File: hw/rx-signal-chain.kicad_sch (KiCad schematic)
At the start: 41 parts, among them T301 BN-43-202, 200 : 3-way 50 ohm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, U301 OPA1692xDGK, U302 SN74LVC04APW, U303 AK5578EN

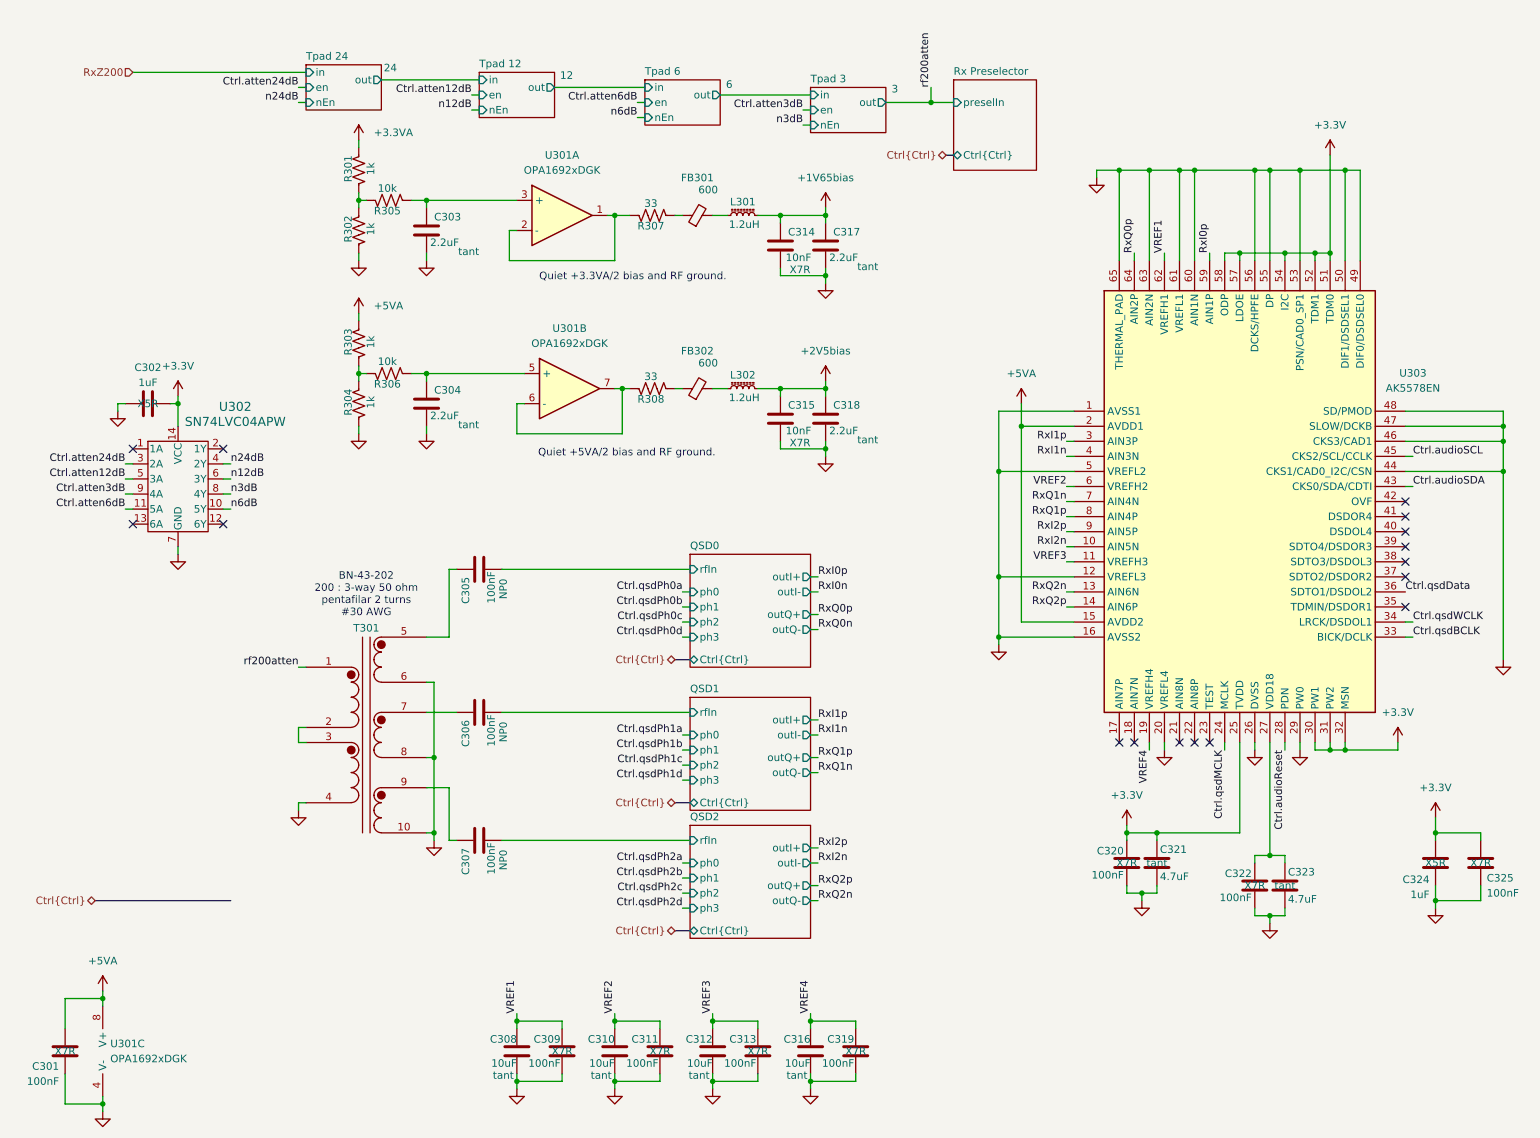
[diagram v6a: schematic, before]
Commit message: All ERC pass. Import to PCB works with no footprints missing.
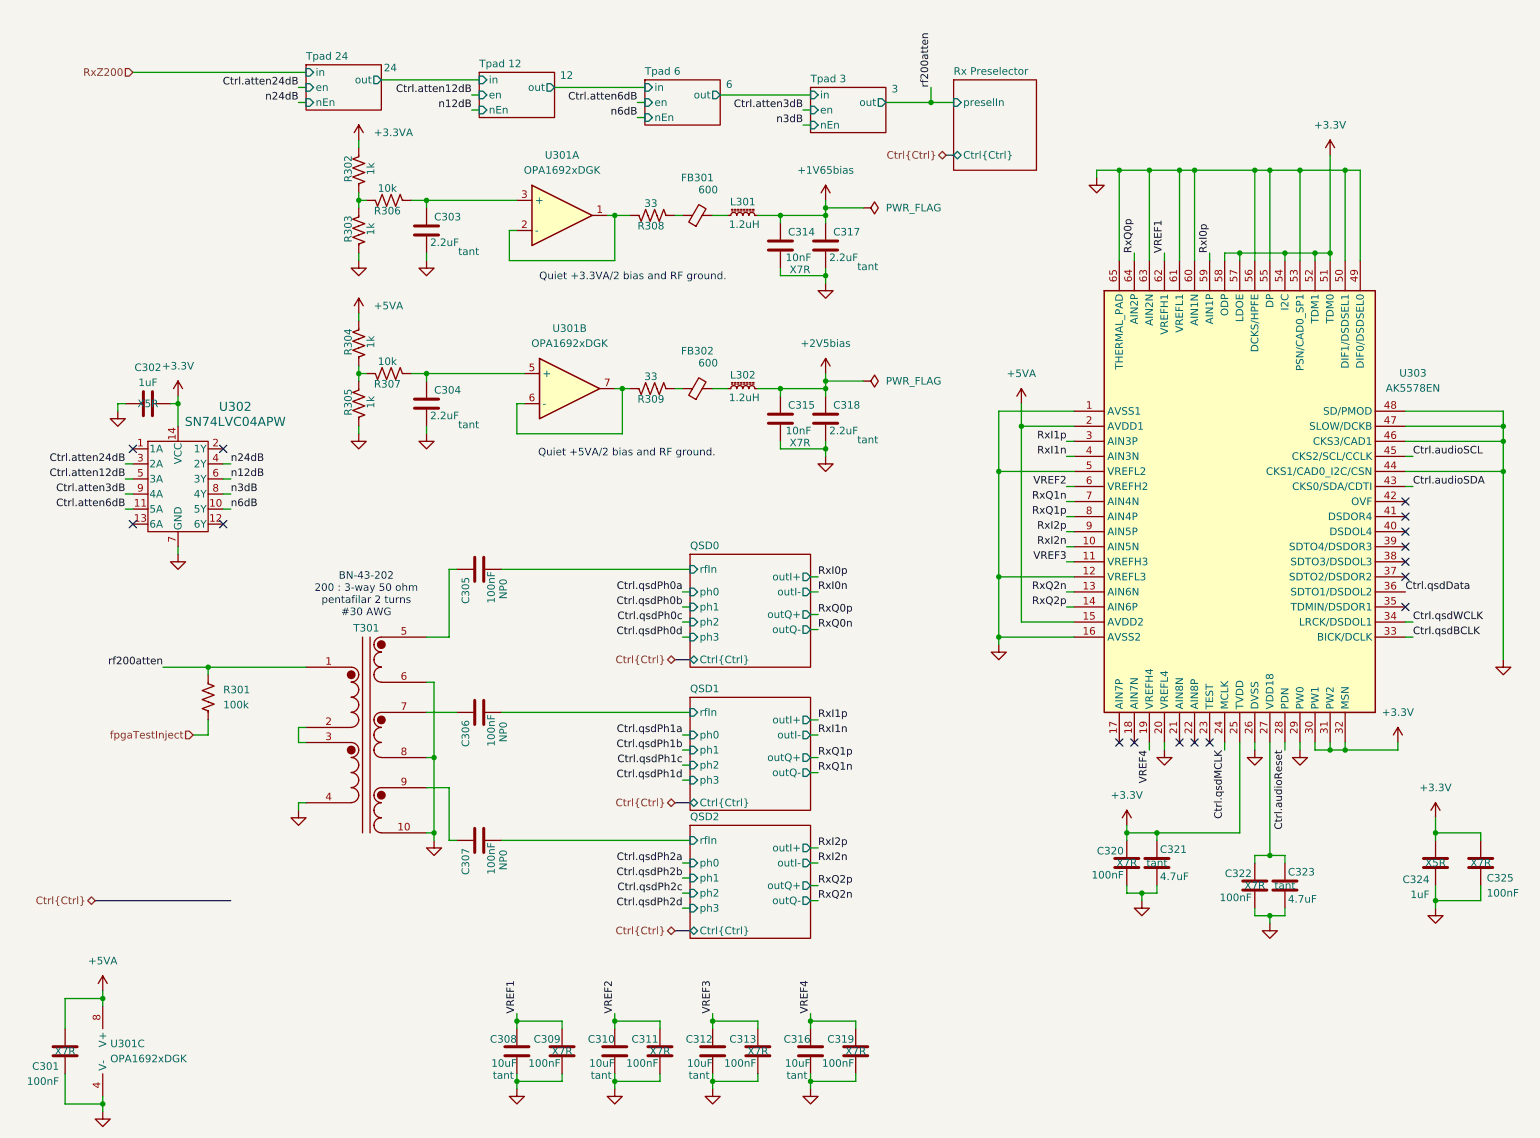
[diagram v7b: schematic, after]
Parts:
- added R301: 100k, Resistor_SMD:R_0402_1005Metric, symbol Device:R_US
- U302: footprint PW14 -> Library:PW14
- U303: symbol AK5578EN:AK5578EN -> Library:AK5578EN
- renumbered R301 to R302, R302 to R303, R303 to R304, R304 to R305, R305 to R306, R306 to R307, R307 to R308, R308 to R309
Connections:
- net rf200atten: now also R301.1
- new net fpgaTestInject: R301.2

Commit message: Checkpoint. Now using TQFP100 STM32H753VIT6, no longer using SPI expanders to drive controls for L,C,atten. FPGA does that now.
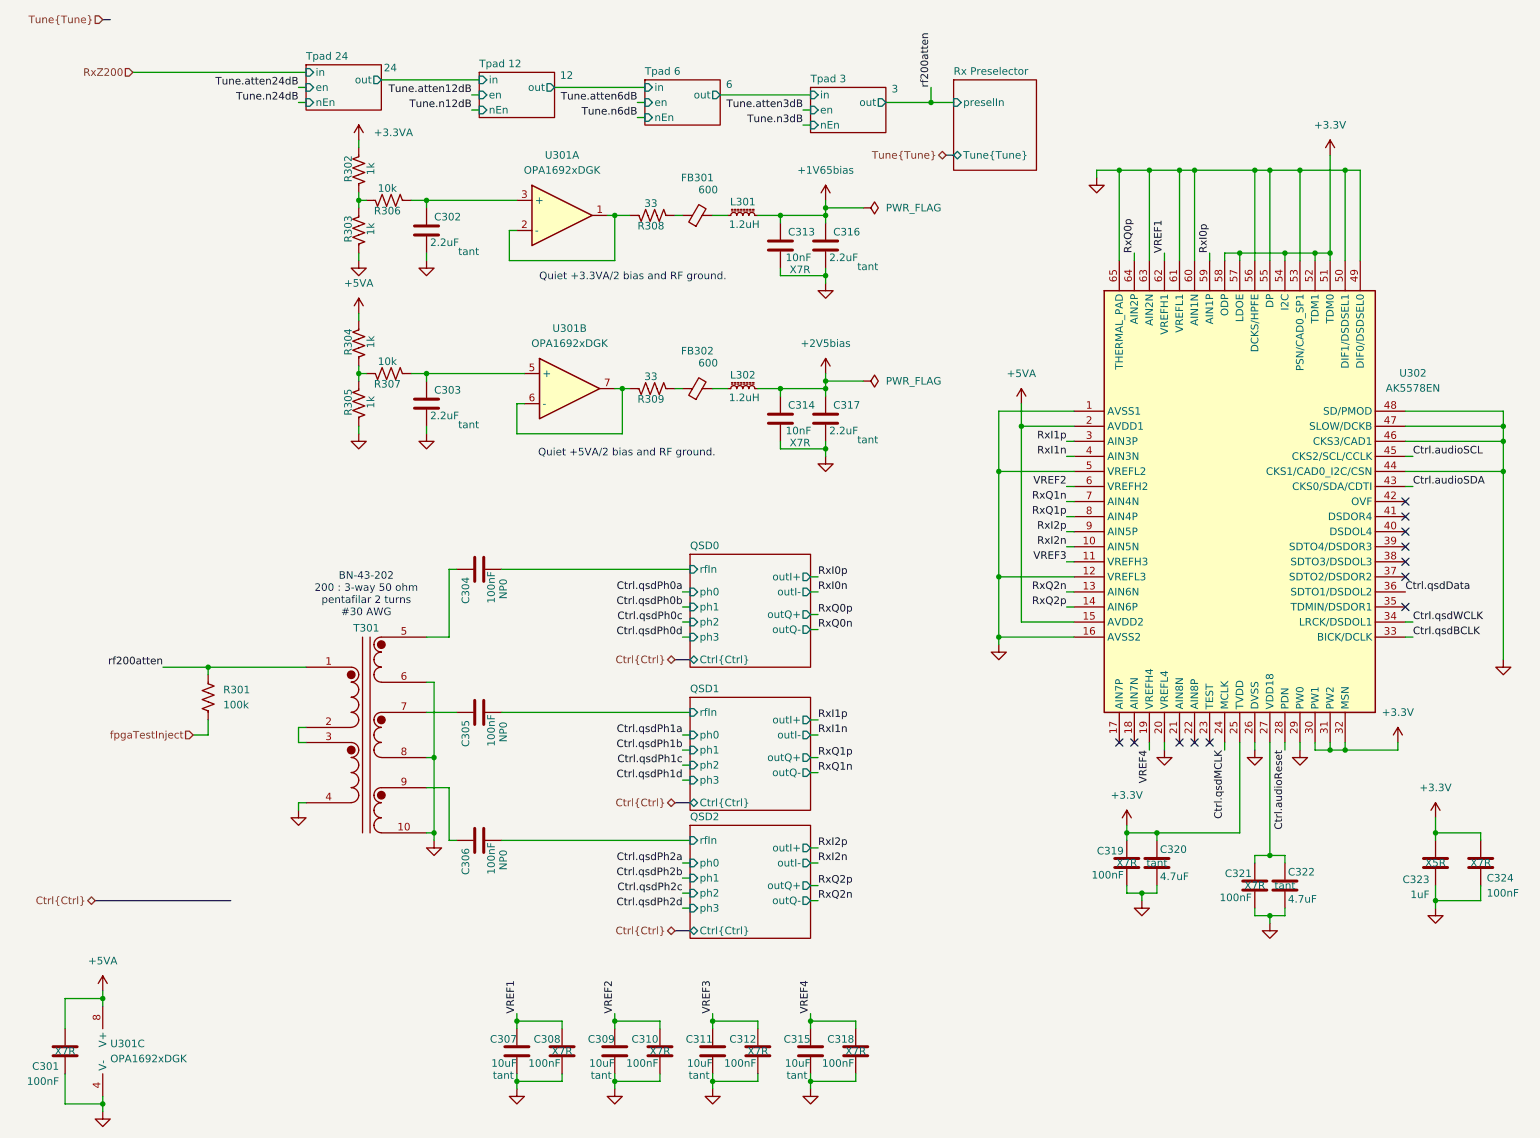
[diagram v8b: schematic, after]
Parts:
- removed C302: 1uF, Capacitor_SMD:C_0402_1005Metric, symbol Device:C
- removed U302: SN74LVC04APW, Library:PW14, symbol Library:SN74LVC04APW
- FB301, FB302: Manufacturer_Name (none) -> Laird Technologies; Manufacturer_Part_Number (none) -> MI0603J601R-10; Mfg Murata -> (none); MfgPN BLM18AG601SN1D -> (none); Mouser Part Number (none) -> 875-MI0603J601R-10
- renumbered C303 to C302, C304 to C303, C305 to C304, C306 to C305, C307 to C306, C308 to C307, C309 to C308, C310 to C309, C311 to C310, C312 to C311, C313 to C312, C314 to C313, C315 to C314, C316 to C315, C317 to C316, C318 to C317, C319 to C318, C320 to C319, C321 to C320, C322 to C321, C323 to C322, C324 to C323, C325 to C324, U303 to U302
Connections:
- no-connect marks 16 -> 12
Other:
- sheet Rx Preselector ports: added Tune{Tune}; removed Ctrl{Ctrl}
